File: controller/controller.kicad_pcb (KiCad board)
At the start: 4 copper layers, 93 x 39 mm, 159 parts, among them J1 Conn_01x14, J2 Conn_01x14, J3 Conn_01x14, J4 Conn_01x14, J5 Conn_01x14, J6 USB_C_Receptacle_USB2.0_16P, J7 USB_C_Receptacle_USB2.0_16P, J8 Conn_01x03_Pin, J9 Conn_01x03_Pin, Q1 BSS138BKS,115, Q2 BSS138BKS,115, Q3 BSS138BKS,115, Q4 FDG6335N, Q5 FDG6335N, Q7 BSS138BKS,115, U1 STM32G474RCTx, U10 PI5C3257, U2 LM5168, U3 TLV76133DCY, U4 TLV76150DCY, U5 ECMF02-2AMX6, U6 ESP32-C6-WROOM-1, U7 ECMF02-2AMX6, U8 PI5C3257, U9 PY32F002AA15M

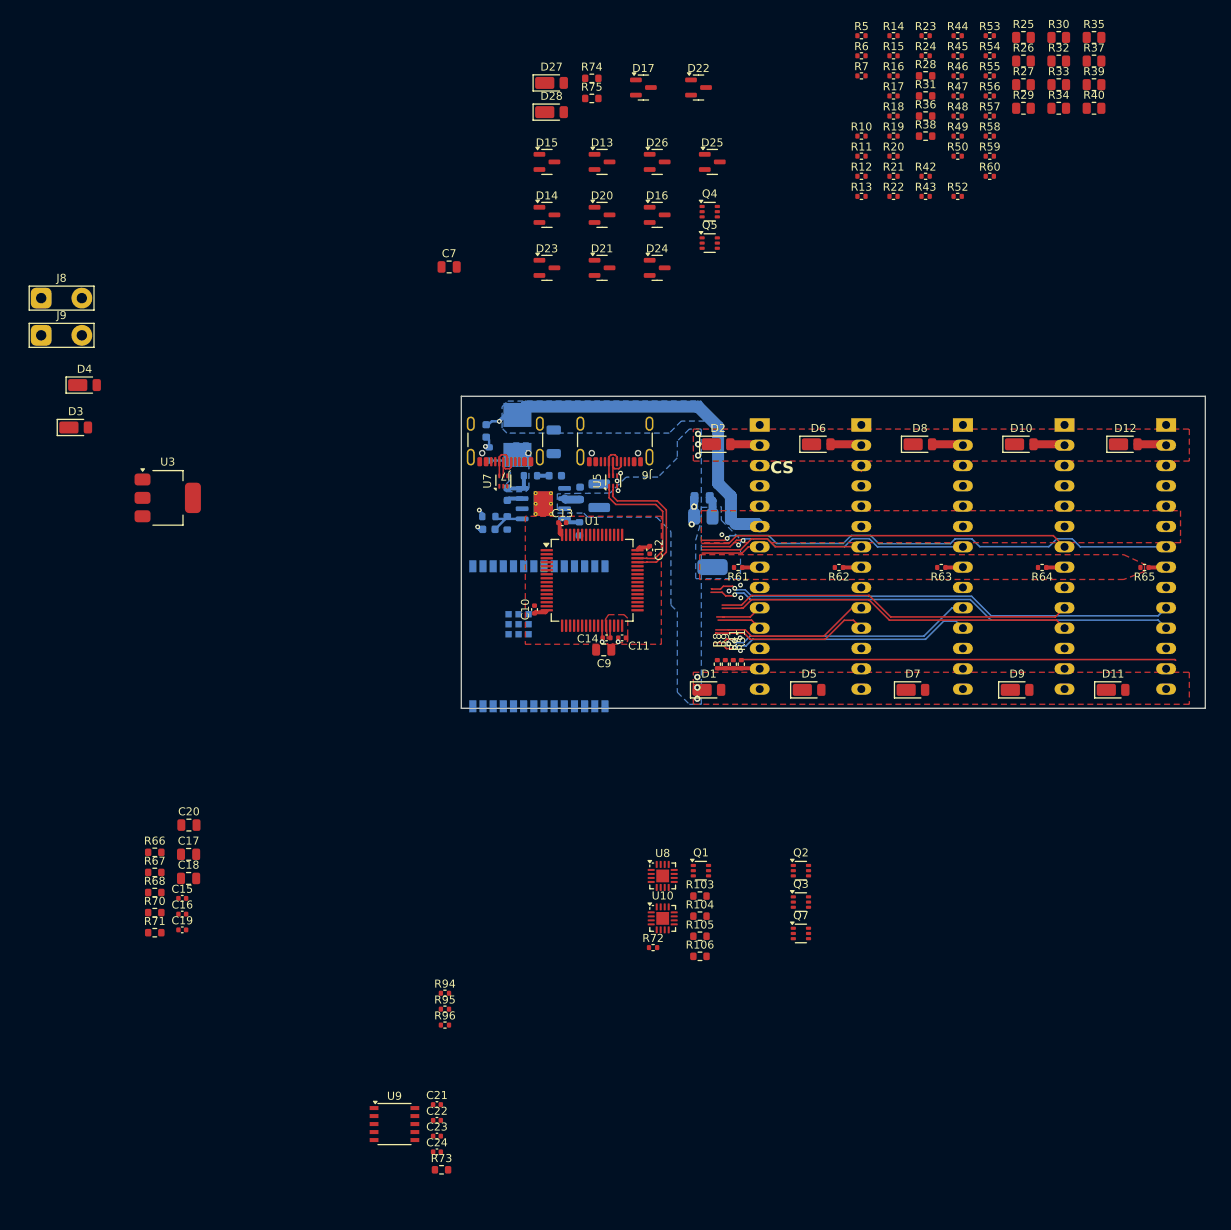
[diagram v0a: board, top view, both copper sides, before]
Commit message: Remove USB CC protections
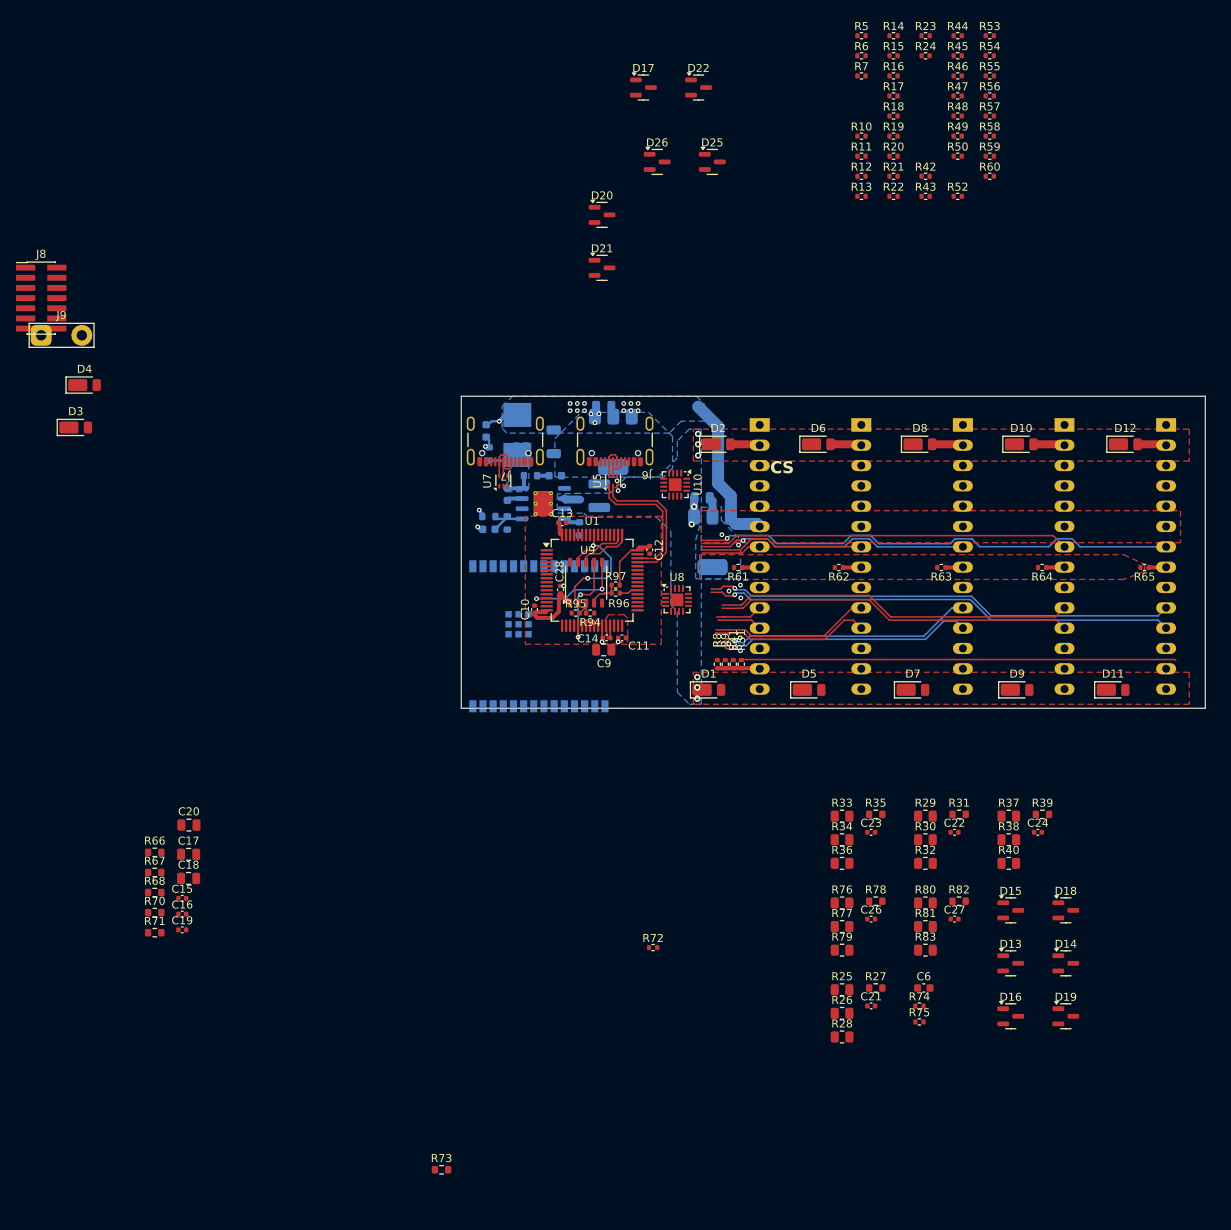
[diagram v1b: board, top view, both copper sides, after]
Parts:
- removed D23, D24: BAT54S, Package_TO_SOT_SMD:SOT-23
- removed D27, D28: DFLS1200, Diode_SMD:D_PowerDI-123
- removed Q1, Q2, Q3, Q7: BSS138BKS,115, Package_TO_SOT_SMD:SOT-363_SC-70-6
- removed Q4, Q5: FDG6335N, Package_TO_SOT_SMD:SOT-363_SC-70-6
- removed R103, R104, R105, R106: 10k, Resistor_SMD:R_0603_1608Metric
- added C26: 100nF, Capacitor_SMD:C_0402_1005Metric, F.Cu at (128.2, 130.4)
- added C27: 100nF, Capacitor_SMD:C_0402_1005Metric, F.Cu at (138.7, 130.4)
- added C28: 100nF, Capacitor_SMD:C_0402_1005Metric, F.Cu at (89.4, 89.2)
- added D18: BAT54S, Package_TO_SOT_SMD:SOT-23, F.Cu at (152.6, 129.3)
- added D19: BAT54S, Package_TO_SOT_SMD:SOT-23, F.Cu at (152.6, 142.5)
- added R76: R_Small, Resistor_SMD:R_0805_2012Metric, F.Cu at (124.6, 128.3)
- added R77: R_Small, Resistor_SMD:R_0805_2012Metric, F.Cu at (124.6, 131.3)
- added R78: R_Small, Resistor_SMD:R_0603_1608Metric, F.Cu at (128.8, 128.1)
- added R79: R_Small, Resistor_SMD:R_0805_2012Metric, F.Cu at (124.6, 134.2)
- added R80: R_Small, Resistor_SMD:R_0805_2012Metric, F.Cu at (135.0, 128.3)
- added R81: R_Small, Resistor_SMD:R_0805_2012Metric, F.Cu at (135.0, 131.3)
- added R82: R_Small, Resistor_SMD:R_0603_1608Metric, F.Cu at (139.2, 128.1)
- added R83: R_Small, Resistor_SMD:R_0805_2012Metric, F.Cu at (135.0, 134.2)
- added R97: 100k, Resistor_SMD:R_0402_1005Metric, F.Cu at (96.3, 88.6)
- C6: moved to F.Cu
- C7, U3: moved to B.Cu
- J8: value Conn_01x03_Pin -> GRPB072VWQS-RC; footprint TestPoint:TestPoint_2Pads_Pitch5.08mm_Drill1.3mm -> Connector_PinHeader_1.27mm:PinHeader_2x07_P1.27mm_Vertical_SMD
- R27, R35, R39: footprint Resistor_SMD:R_0805_2012Metric -> Resistor_SMD:R_0603_1608Metric
- R28, R36, R38: footprint Resistor_SMD:R_0603_1608Metric -> Resistor_SMD:R_0805_2012Metric
- R74, R75: value 1k -> 0R; footprint Resistor_SMD:R_0603_1608Metric -> Resistor_SMD:R_0402_1005Metric
- moved R74 123.0 mm to (134.3, 141.2)
- moved R75 122.5 mm to (134.3, 143.2)
- moved R25 121.2 mm to (124.6, 139.2)
- moved R26 121.2 mm to (124.6, 142.1)
- moved R28 120.6 mm to (124.6, 145.1)
- moved R27 114.4 mm to (128.8, 139.0)
- moved D14 113.8 mm to (152.6, 135.9)
- moved D13 112.4 mm to (145.7, 135.9)
- moved D15 110.1 mm to (145.7, 129.3)
- moved D16 109.5 mm to (145.7, 142.5)
- moved R30 101.7 mm to (135.0, 120.4)
- moved R32 101.7 mm to (135.0, 123.4)
- moved R35 100.9 mm to (128.8, 117.3)
- moved R33 95.4 mm to (124.6, 117.5)
- moved R34 95.4 mm to (124.6, 120.4)
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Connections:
- C21 pad 1: /FB_A -> /FB_B
- C22 pad 1: /FB_B -> /FB_C
- C23 pad 1: /FB_C -> /FB_D
- C24 pad 1: /FB_D -> /PA4
- C6 pad 1: Logic DC/DC in -> Net-(D3-A)
- D13 pad 3: /FB_D -> /FB_B
- D15 pad 3: /FB_B -> /FB_D
- D16 pad 3: /FB_A -> /PA4
- J6 pad S1: unconnected-(J6-SHIELD-PadS1) -> Earth
- J7 pad S1: unconnected-(J7-SHIELD-PadS1) -> Earth
- J8 pad 1: FB_LOW -> Net-(D3-A)
- R25 pad 1: FB_A_FULL -> FB_B_FULL
- R25 pad 2: /FB_A -> /FB_B
- R26 pad 1: FB_A_FULL -> FB_B_FULL
- R26 pad 2: /FB_A -> /FB_B
- R27 pad 1: FB_A_FULL -> /FB_B
- R27 pad 2: /FB_A -> Earth
- R28 pad 1: /FB_A -> FB_B_FULL
- R28 pad 2: Earth -> /FB_B
- R29 pad 1: FB_B_FULL -> FB_C_FULL
- R29 pad 2: /FB_B -> /FB_C
- R30 pad 1: FB_B_FULL -> FB_C_FULL
- R30 pad 2: /FB_B -> /FB_C
- R31 pad 1: /FB_B -> /FB_C
- R32 pad 1: FB_B_FULL -> FB_C_FULL
- R32 pad 2: /FB_B -> /FB_C
- R33 pad 1: FB_C_FULL -> FB_D_FULL
- R33 pad 2: /FB_C -> /FB_D
- R35 pad 1: FB_C_FULL -> /FB_D
- R35 pad 2: /FB_C -> Earth
- R36 pad 1: /FB_C -> FB_D_FULL
- R36 pad 2: Earth -> /FB_D
- R37 pad 1: FB_D_FULL -> /48V to 3v3 div_0/IN
- R37 pad 2: /FB_D -> /PA4
- R38 pad 1: /FB_D -> /48V to 3v3 div_0/IN
- R38 pad 2: Earth -> /PA4
- R39 pad 1: FB_C_FULL -> /PA4
- R39 pad 2: /FB_C -> Earth
- R40 pad 1: FB_D_FULL -> /48V to 3v3 div_0/IN
- R40 pad 2: /FB_D -> /PA4
- R74 pad 1: Net-(D18-A) -> Net-(D1-A)
- R74 pad 2: /~{EN_CC2} -> /48V to 3v3 div_0/IN
- R75 pad 1: Net-(D19-A) -> Net-(D2-A)
- R75 pad 2: /~{EN_CC1} -> /48V to 3v3 div_5/IN
- R96 pad 1: Net-(J13-~{RESET}) -> /STM32_NRST_TO_CON
- U1 pad 18: ADC2_IN17 -> /PA4
- U1 pad 19: /FRS2 -> /PA5
- U1 pad 2: /EN_CC1 -> /~{EN_CC}
- U1 pad 3: /EN_CC2 -> /CC_SELECT
- U1 pad 52: /EN_VCONN1 -> /~{EN_VCONN}
- U1 pad 53: /EN_VCONN2 -> unconnected-(U1-PC11-Pad53)
- U1 pad 54: /FRS1 -> /FRS
- U9 pad 4: Net-(J13-~{RESET}) -> /STM32_NRST_TO_CON
- U9 pad 8: Net-(J13-SWDIO/TMS) -> /STM32_SWDIO
- U9 pad 9: Net-(J13-SWCLK/TCK) -> /STM32_SWC
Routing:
- net 6-18V: track 60.6 -> 37.6 mm, vias 2 -> 14
- net /STM32_TX: track 0.00 -> 13.6 mm, vias 0 -> 2
- net +3V3: track 6.56 -> 20.1 mm
- net /FB_A: track 0.00 -> 13.3 mm, vias 0 -> 2
- net /FB_B: track 0.00 -> 12.3 mm, vias 0 -> 2
- net /STM32_SWC: track 0.00 -> 7.21 mm
- net /STM32_SWDIO: track 0.00 -> 6.81 mm
- net /STM32_NRST_TO_CON: track 0.00 -> 4.00 mm
- net Net-(U9-Pin_3): track 0.00 -> 2.83 mm
- net /HI_1: track 5.63 -> 7.99 mm
- net Earth: vias 15 -> 19
- added copper zone on B.Cu, net +3V3
- added copper zone on In2.Cu, net 6-18V

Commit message: Controller - Try to simplify
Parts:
- removed D13, D14, D15, D16, D17, D18, D19, D20, D21, D22, D25, D26: BAT54S, Package_TO_SOT_SMD:SOT-23
- removed R10, R11, R12, R19, R20, R21, R22, R47, R48, R49, R50, R57, R58, R59, R60, R64, R65, R7: 0R, Resistor_SMD:R_0402_1005Metric
- added R100: 0R, Resistor_SMD:R_0402_1005Metric, F.Cu at (153.4, 46.6)
- added R101: 0R, Resistor_SMD:R_0402_1005Metric, F.Cu at (153.4, 48.6)
- added R102: 0R, Resistor_SMD:R_0402_1005Metric, F.Cu at (156.3, 44.6)
- added R103: 0R, Resistor_SMD:R_0402_1005Metric, F.Cu at (156.3, 46.6)
- added R104: 0R, Resistor_SMD:R_0402_1005Metric, F.Cu at (156.3, 48.6)
- added R105: 0R, Resistor_SMD:R_0402_1005Metric, F.Cu at (159.2, 44.6)
- added R106: 0R, Resistor_SMD:R_0402_1005Metric, F.Cu at (159.2, 46.6)
- added R107: 0R, Resistor_SMD:R_0402_1005Metric, F.Cu at (159.2, 48.6)
- added R84: 0R, Resistor_SMD:R_0402_1005Metric, F.Cu at (153.4, 36.6)
- added R86: 0R, Resistor_SMD:R_0402_1005Metric, F.Cu at (153.4, 38.6)
- added R87: 0R, Resistor_SMD:R_0402_1005Metric, F.Cu at (153.4, 40.6)
- added R88: 0R, Resistor_SMD:R_0402_1005Metric, F.Cu at (156.3, 36.6)
- added R89: 0R, Resistor_SMD:R_0402_1005Metric, F.Cu at (156.3, 38.6)
- added R90: 0R, Resistor_SMD:R_0402_1005Metric, F.Cu at (153.4, 44.6)
- added R91: 0R, Resistor_SMD:R_0402_1005Metric, F.Cu at (156.3, 40.6)
- added R92: 0R, Resistor_SMD:R_0402_1005Metric, F.Cu at (159.2, 36.6)
- added R93: 0R, Resistor_SMD:R_0402_1005Metric, F.Cu at (159.2, 38.6)
- added R99: 0R, Resistor_SMD:R_0402_1005Metric, F.Cu at (159.2, 40.6)
- added U11: QSBT40-7-F, Package_TO_SOT_SMD:SOT-363_SC-70-6, F.Cu at (105.3, 77.0)
- added U12: QSBT40-7-F, Package_TO_SOT_SMD:SOT-363_SC-70-6, F.Cu at (87.5, 95.0)
- added U13: QSBT40-7-F, Package_TO_SOT_SMD:SOT-363_SC-70-6, F.Cu at (90.3, 97.5)
- J8: moved to B.Cu
- moved D12 125.8 mm to (36.8, 46.0)
- moved D11 123.4 mm to (37.8, 76.1)
- moved D3 99.6 mm to (123.0, 101.1)
- moved D4 92.0 mm to (121.6, 71.0)
- moved J8 84.0 mm to (107.1, 68.2), turned to 90 degrees
- moved R41 76.6 mm to (169.1, 48.6)
- moved R51 76.6 mm to (170.1, 48.6)
- moved R8 76.6 mm to (167.1, 48.6)
- moved R9 76.6 mm to (168.1, 48.6)
- moved D5 15.5 mm to (136.0, 101.1)
- moved D7 15.5 mm to (149.0, 101.1)
- moved D9 14.6 mm to (161.1, 101.1)
- moved D8 13.0 mm to (147.3, 71.0)
- moved D10 12.9 mm to (159.9, 71.0)
- moved D6 12.9 mm to (134.6, 71.0)
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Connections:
- C6 pad 1: Net-(D3-A) -> Net-(D11-A)
- D1 pad 2: Net-(D1-A) -> /hb-card1/FB_x_FULL_HI
- D10 pad 2: Net-(D10-A) -> /hb-card5/FB_x_FULL_LO
- D2 pad 2: Net-(D2-A) -> /hb-card1/FB_x_FULL_LO
- D3 pad 2: Net-(D3-A) -> /hb-card2/FB_x_FULL_HI
- D4 pad 2: Net-(D4-A) -> /hb-card2/FB_x_FULL_LO
- D5 pad 2: Net-(D5-A) -> /hb-card3/FB_x_FULL_HI
- D6 pad 2: Net-(D6-A) -> /hb-card3/FB_x_FULL_LO
- D7 pad 2: Net-(D7-A) -> /hb-card4/FB_x_FULL_HI
- D8 pad 2: Net-(D8-A) -> /hb-card4/FB_x_FULL_LO
- D9 pad 2: Net-(D9-A) -> /hb-card5/FB_x_FULL_HI
- J1 pad 13: Net-(D1-A) -> /hb-card1/FB_x_FULL_HI
- J1 pad 2: Net-(D2-A) -> /hb-card1/FB_x_FULL_LO
- J2 pad 13: Net-(D5-A) -> /hb-card2/FB_x_FULL_HI
- J2 pad 2: Net-(D6-A) -> /hb-card2/FB_x_FULL_LO
- J3 pad 13: Net-(D7-A) -> /hb-card3/FB_x_FULL_HI
- J3 pad 2: Net-(D8-A) -> /hb-card3/FB_x_FULL_LO
- J3 pad 3: unconnected-(J3-Pin_3-Pad3) -> /Current_sense_3B
- J4 pad 13: Net-(D9-A) -> /hb-card4/FB_x_FULL_HI
- J4 pad 2: Net-(D10-A) -> /hb-card4/FB_x_FULL_LO
- J5 pad 13: Net-(D11-A) -> /hb-card5/FB_x_FULL_HI
- J5 pad 2: Net-(D12-A) -> /hb-card5/FB_x_FULL_LO
- J6 pad A4: Net-(D3-A) -> Net-(D11-A)
- J6 pad A9: Net-(D3-A) -> Net-(D11-A)
- J6 pad B4: Net-(D3-A) -> Net-(D11-A)
- J6 pad B9: Net-(D3-A) -> Net-(D11-A)
- J7 pad A4: Net-(D4-A) -> Net-(D12-A)
- J7 pad A9: Net-(D4-A) -> Net-(D12-A)
- J7 pad B4: Net-(D4-A) -> Net-(D12-A)
- J7 pad B9: Net-(D4-A) -> Net-(D12-A)
- J8 pad 1: Net-(D3-A) -> Net-(D11-A)
- J8 pad 10: Earth -> +3V3
- J8 pad 2: Net-(D3-A) -> Net-(D11-A)
- J8 pad 3: Net-(D3-A) -> 6-18V
- J9 pad 2: Net-(D4-A) -> Net-(D12-A)
- R13 pad 1: Net-(D2-A) -> /hb-card3/FB_x_FULL_HI
- R13 pad 2: FB_A_FULL -> FB_D_FULL
- R14 pad 1: Net-(D2-A) -> /hb-card3/FB_x_FULL_LO
- R14 pad 2: FB_B_FULL -> FB_A_FULL
- R15 pad 1: Net-(D6-A) -> /hb-card3/FB_x_FULL_LO
- R15 pad 2: FB_A_FULL -> FB_B_FULL
- R16 pad 1: Net-(D6-A) -> /hb-card3/FB_x_FULL_LO
- R16 pad 2: FB_B_FULL -> FB_C_FULL
- R17 pad 1: Net-(D8-A) -> Net-(J4-Pin_8)
- R17 pad 2: FB_A_FULL -> +5V
- R18 pad 1: Net-(D8-A) -> /hb-card4/FB_x_FULL_HI
- R18 pad 2: FB_B_FULL -> FB_A_FULL
- R23 pad 1: Net-(D7-A) -> /hb-card4/FB_x_FULL_HI
- R23 pad 2: FB_A_FULL -> FB_B_FULL
- R24 pad 1: Net-(D7-A) -> /hb-card4/FB_x_FULL_HI
- R24 pad 2: FB_B_FULL -> FB_C_FULL
- R41 pad 1: Net-(D1-A) -> /hb-card3/FB_x_FULL_LO
- R41 pad 2: FB_C_FULL -> FB_D_FULL
- R42 pad 1: Net-(D2-A) -> /hb-card4/FB_x_FULL_HI
- R42 pad 2: FB_C_FULL -> FB_D_FULL
- R43 pad 1: Net-(D5-A) -> /hb-card4/FB_x_FULL_LO
- R43 pad 2: FB_C_FULL -> FB_A_FULL
- R44 pad 1: Net-(D5-A) -> /hb-card4/FB_x_FULL_LO
- R44 pad 2: FB_D_FULL -> FB_B_FULL
- R45 pad 1: Net-(D7-A) -> /hb-card4/FB_x_FULL_LO
- R46 pad 1: Net-(D7-A) -> /hb-card4/FB_x_FULL_LO
- R5 pad 1: Net-(D5-A) -> Net-(J3-Pin_8)
- R5 pad 2: FB_A_FULL -> +5V
- R51 pad 1: Net-(D1-A) -> Net-(J5-Pin_8)
- R51 pad 2: FB_D_FULL -> +5V
- R52 pad 1: Net-(D2-A) -> /hb-card5/FB_x_FULL_HI
- R52 pad 2: FB_D_FULL -> FB_A_FULL
- R53 pad 1: Net-(D6-A) -> /hb-card5/FB_x_FULL_HI
- R53 pad 2: FB_C_FULL -> FB_B_FULL
- R54 pad 1: Net-(D6-A) -> /hb-card5/FB_x_FULL_HI
- R54 pad 2: FB_D_FULL -> FB_C_FULL
- R55 pad 1: Net-(D8-A) -> /hb-card5/FB_x_FULL_HI
- R55 pad 2: FB_C_FULL -> FB_D_FULL
- R56 pad 1: Net-(D8-A) -> /hb-card5/FB_x_FULL_LO
- R56 pad 2: FB_D_FULL -> FB_A_FULL
- R6 pad 1: Net-(D5-A) -> /hb-card3/FB_x_FULL_HI
- R6 pad 2: FB_B_FULL -> FB_A_FULL
- R61 pad 1: Net-(J1-Pin_8) -> /hb-card5/FB_x_FULL_LO
- R61 pad 2: +5V -> FB_B_FULL
- R62 pad 1: Net-(J2-Pin_8) -> /hb-card5/FB_x_FULL_LO
- R62 pad 2: +5V -> FB_C_FULL
- R63 pad 1: Net-(J3-Pin_8) -> /hb-card5/FB_x_FULL_LO
- R63 pad 2: +5V -> FB_D_FULL
- R74 pad 1: Net-(D1-A) -> /hb-card1/FB_x_FULL_LO
- R75 pad 1: Net-(D2-A) -> /hb-card1/FB_x_FULL_HI
- R8 pad 1: Net-(D1-A) -> /hb-card3/FB_x_FULL_HI
- R8 pad 2: FB_A_FULL -> FB_B_FULL
- R9 pad 1: Net-(D1-A) -> /hb-card3/FB_x_FULL_HI
- R9 pad 2: FB_B_FULL -> FB_C_FULL
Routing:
- net FB_D_FULL: track 54.4 -> 0.00 mm
- net /~{EN_CC}: track 0.00 -> 32.1 mm, vias 0 -> 3
- net /CC2_MCU: track 0.00 -> 23.9 mm, vias 0 -> 3
- net /FRS: track 0.00 -> 23.7 mm, vias 0 -> 3
- net /CC1_MCU: track 0.00 -> 22.9 mm, vias 0 -> 3
- net /~{EN_VCONN}: track 0.00 -> 19.2 mm, vias 0 -> 3
- net /CC2: track 0.00 -> 17.9 mm, vias 0 -> 1
- net /CC1: track 0.00 -> 15.1 mm, vias 0 -> 1
- net 6-18V: track 37.6 -> 30.8 mm
- net Net-(D1-A): track 5.32 -> 0.00 mm
- net Net-(D8-A): track 4.49 -> 0.00 mm
- net /hb-card3/FB_x_FULL_LO: track 0.00 -> 4.49 mm
- net Net-(D2-A): track 4.14 -> 0.00 mm
- net /hb-card1/FB_x_FULL_LO: track 0.00 -> 4.14 mm
- net Net-(D10-A): track 3.92 -> 0.00 mm
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- added copper zone on B.Cu, net Net-(D11-A)
- added copper zone on F.Cu, net Net-(D11-A)
- added copper zone on In2.Cu, net Net-(D11-A)

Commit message: Controller - More work mainly on layout
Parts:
- removed R25, R26, R28, R29, R30, R32, R33, R34, R36, R37, R38, R40, R76, R77, R79, R80, R81, R83: R_Small, Resistor_SMD:R_0805_2012Metric
- C21, C22, C23, C24, C26, C27: footprint Capacitor_SMD:C_0402_1005Metric -> Capacitor_SMD:C_0402_1005Metric_Pad0.74x0.62mm_HandSolder
- R100, R101, R102, R103, R104, R105, R106, R107, R13, R14, R15, R16, R18, R23, R24, R41, R42, R43, R44, R45, R46, R52, R53, R54, R55, R56, R6, R61, R62, R63, R8, R86, R87, R88, R89, R9, R91, R92, R93, R99: footprint Resistor_SMD:R_0402_1005Metric -> Resistor_SMD:R_0805_2012Metric
- R27, R31, R35, R39, R78, R82: footprint Resistor_SMD:R_0603_1608Metric -> Resistor_SMD:R_0402_1005Metric_Pad0.72x0.64mm_HandSolder
- moved R53 80.8 mm to (161.2, 98.7), turned to 90 degrees
- moved R23 79.9 mm to (148.6, 98.7), turned to 90 degrees
- moved R54 78.2 mm to (160.2, 98.7), turned to 90 degrees
- moved R88 77.6 mm to (109.5, 98.6), turned to 90 degrees
- moved R24 77.3 mm to (147.6, 98.7), turned to 90 degrees
- moved R6 76.9 mm to (137.0, 98.7), turned to 90 degrees
- moved R89 76.7 mm to (108.5, 98.6), turned to 90 degrees
- moved R55 75.5 mm to (159.2, 98.7), turned to 90 degrees
- moved C6 73.3 mm to (99.1, 74.9), turned to 45 degrees
- moved R86 73.1 mm to (111.5, 98.6), turned to 90 degrees
- moved R87 72.1 mm to (110.5, 98.6), turned to 90 degrees
- moved R18 71.2 mm to (149.6, 98.7), turned to 90 degrees
- moved R5 67.2 mm to (137.0, 86.4), turned to 180 degrees
- moved R84 65.0 mm to (111.6, 86.4), turned to 180 degrees
- moved R102 63.7 mm to (122.4, 98.6), turned to 90 degrees
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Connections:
- C21 pad 1: /FB_B -> FB_B_FULL
- C22 pad 1: /FB_C -> FB_C_FULL
- C23 pad 1: /FB_D -> FB_D_FULL
- C26 pad 1: /FB_A -> FB_A_FULL
- R27 pad 1: /FB_B -> FB_B_FULL
- R31 pad 1: /FB_C -> FB_C_FULL
- R35 pad 1: /FB_D -> FB_D_FULL
- R74 pad 2: /48V to 3v3 div_0/IN -> /PA4
- R75 pad 2: /48V to 3v3 div_5/IN -> /PA5
- R78 pad 1: /FB_A -> FB_A_FULL
- U1 pad 13: /FB_A -> FB_A_FULL
- U1 pad 20: /FB_C -> FB_C_FULL
- U1 pad 21: /FB_B -> FB_B_FULL
- U1 pad 9: /FB_D -> FB_D_FULL
- U12 pad 1: /FB_D -> FB_D_FULL
- U12 pad 3: /FB_C -> FB_C_FULL
- U12 pad 4: /FB_B -> FB_B_FULL
- U12 pad 6: /FB_A -> FB_A_FULL
- U9 pad 6: /FB_A -> FB_A_FULL
- U9 pad 7: /FB_B -> FB_B_FULL
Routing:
- net /Current_sense_5A: track 0.00 -> 58.7 mm
- net FB_A_FULL: track 0.00 -> 58.2 mm, vias 0 -> 7
- net /Current_sense_5B: track 0.00 -> 57.9 mm, vias 0 -> 1
- net FB_B_FULL: track 0.00 -> 55.2 mm, vias 0 -> 7
- net FB_D_FULL: track 0.00 -> 46.3 mm, vias 0 -> 5
- net /Current_sense_4A: track 0.00 -> 46.0 mm
- net /Current_sense_4B: track 0.00 -> 44.3 mm, vias 0 -> 1
- net FB_C_FULL: track 0.00 -> 43.0 mm, vias 0 -> 5
- net /Current_sense_3B: track 0.00 -> 37.9 mm, vias 0 -> 1
- net /Current_sense_3A: track 0.00 -> 33.8 mm
- net /Current_sense_2A: track 0.00 -> 27.5 mm, vias 0 -> 3
- net /Current_sense_2B: track 0.74 -> 25.9 mm, vias 0 -> 3
- net /FB_A: track 13.3 -> 0.00 mm, vias 2 -> 0
- net /FB_B: track 12.3 -> 0.00 mm, vias 2 -> 0
- net /Current_sense_1A: track 0.00 -> 10.8 mm, vias 0 -> 1
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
